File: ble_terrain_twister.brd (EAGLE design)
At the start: 26.8 x 15.5 mm, 14 parts, among them IC1 UA78M33DCY

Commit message: Finished routing. again.
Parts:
- removed BRD1: TERRAIN_TWISTER_EDGEEDGE, terrain_twister_control_board_edge:TERRAIN_TWISTER_CONTROL_BRD_EDGE
- added JP1: (no value), SparkFun:1X08_1.27MM
- added JP2: LEFT_PH, terrain_twister_control_board_edge:1X08_1.27MM
- added LED1, LED2: LED0603, CEDT:CHIPLED_0603
- added R1, R2: 100, rcl:R0603
- U1: value (none) -> YJ-14015
- moved R6 49.7 mm to (30.4, 13.6)
- moved R7 49.7 mm to (30.4, 15.8)
- moved IC1 49.4 mm to (25.6, 21.1)
- moved SWD 49.4 mm to (30.5, 21.9)
- moved C4 49.4 mm to (24.2, 15.8)
- moved C6 49.4 mm to (27.2, 15.8)
- moved C5 49.4 mm to (24.2, 13.6)
- moved C7 49.4 mm to (27.2, 13.6)
- moved U1 47.1 mm to (20.2, 13.1)
- moved C2 41.9 mm to (16.2, 15.4), flipped to the bottom
- moved C8 40.8 mm to (16.2, 18.5), flipped to the bottom, turned to 270 degrees
- moved C1 38.7 mm to (18.4, 15.4), turned to 90 degrees
- moved C3 35.6 mm to (20.5, 15.4), flipped to the bottom
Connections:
- new net N$1: LED1.C, R1.2
- new net N$2: LED2.C, R2.2
- new net STATUS_LED_A: LED1.A, U1.P.11
- new net STATUS_LED_B: LED2.A, U1.P.12
- net A: now also JP1.4; no longer BRD1.5
- net B: now also JP2.7, U1.P.03; no longer BRD1.15, U1.P.04
- net C: now also JP1.7; no longer BRD1.2
- net GND: now also JP1.8, R1.1, R2.1; no longer BRD1.1
- net M1+: now also JP2.6, U1.P.02; no longer BRD1.14, U1.P.11
- net M1-: now also JP2.5, U1.P.01; no longer BRD1.13, U1.P.12
- net M2+: now also JP1.2; no longer BRD1.7
- net M2-: now also JP1.3; no longer BRD1.6
- net M3+: now also JP1.5; no longer BRD1.4
- net M3-: now also JP1.6; no longer BRD1.3
- net SW2: now also JP2.2, U1.P.00; no longer BRD1.10, U1.P.13
- net SW3: now also JP2.1, U1.P.30; no longer BRD1.9, U1.P.14
- net VBAT: now also JP1.1; no longer BRD1.8
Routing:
- net VCC: track 47.3 -> 28.3 mm
- net VBAT: track 11.8 -> 27.8 mm
- net M2+: track 5.79 -> 18.9 mm
- net A: track 19.7 -> 8.88 mm
- net M1-: track 12.6 -> 3.62 mm
- net M1+: track 11.8 -> 3.69 mm
- net SW3: track 9.86 -> 3.74 mm
- net SW2: track 9.17 -> 3.34 mm
- net C: track 4.82 -> 9.44 mm, vias 1 -> 0
- net M2-: track 18.9 -> 16.1 mm
- net M3+: track 14.7 -> 12.2 mm, vias 1 -> 0
- net SWDIO: track 4.69 -> 2.41 mm
- net M3-: track 12.4 -> 10.3 mm, vias 1 -> 0
- net N$1: track 0.00 -> 1.92 mm
- net SWDCLK: track 5.29 -> 3.45 mm
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- added copper zone on layer 1, net GND
- added copper zone on layer 16, net GND
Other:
- board size 26.8 x 15.5 mm -> 20.6 x 19.8 mm
- board text added: "M.M. 2017"
- board text removed: "Daughterboard key slot"
- board text removed: "Factory PCB top"

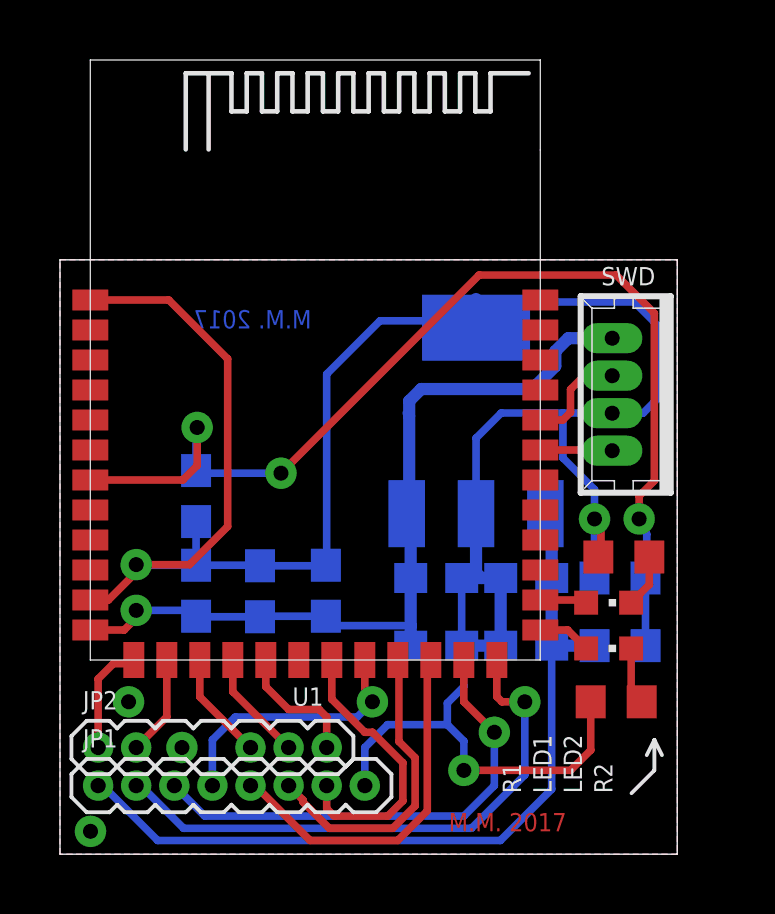
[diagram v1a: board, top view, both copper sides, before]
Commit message: YJ-14015 footprint fixed
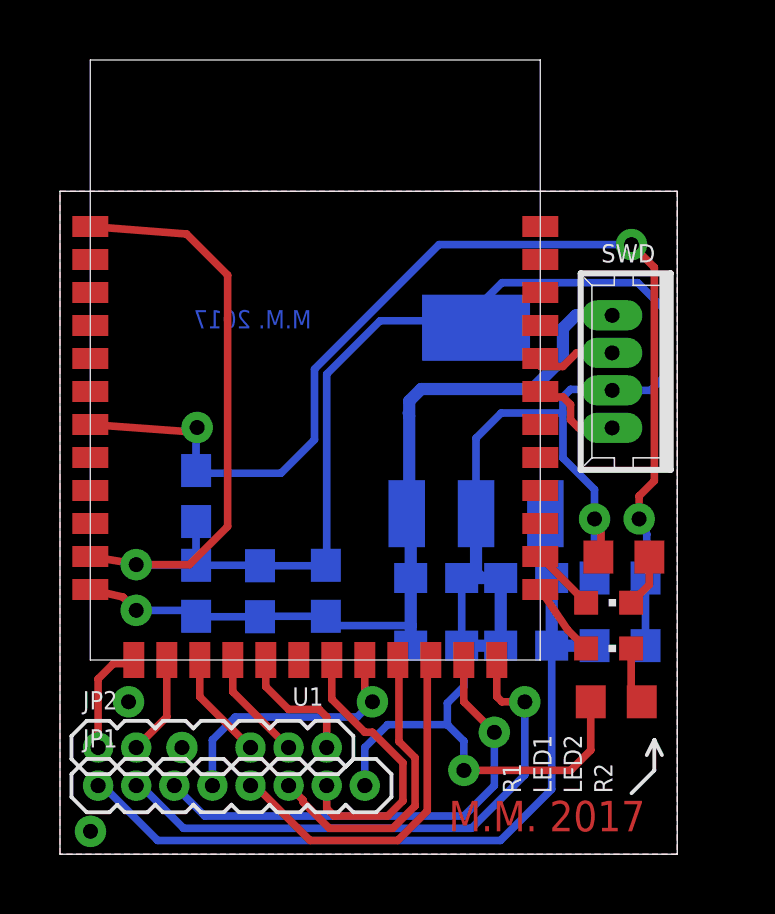
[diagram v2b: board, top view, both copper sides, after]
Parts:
- moved SWD 0.76 mm to (30.5, 22.7)
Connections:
- net N$1 renamed LED_A_R
- net N$2 renamed LED_B_R
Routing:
- net GND: track 92.1 -> 95.1 mm
- net VBAT_ADC: track 36.9 -> 38.6 mm
- net SWDIO: track 2.41 -> 3.25 mm
- net STATUS_LED_A: track 1.78 -> 2.50 mm
- net SWDCLK: track 3.45 -> 2.84 mm
- net STATUS_LED_B: track 1.57 -> 2.17 mm
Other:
- board size 20.6 x 19.8 mm -> 20.6 x 22.1 mm
